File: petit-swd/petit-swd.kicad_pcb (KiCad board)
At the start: 2 copper layers, 11 parts, among them CON101 302-S201, CON102 61300411121, CON103 PPTC041LGBN-RC, CON104 USB-B1HSB6, CON105 61300311121, CON106 61300211121, U101 AZ1117CH-3.3TRG1

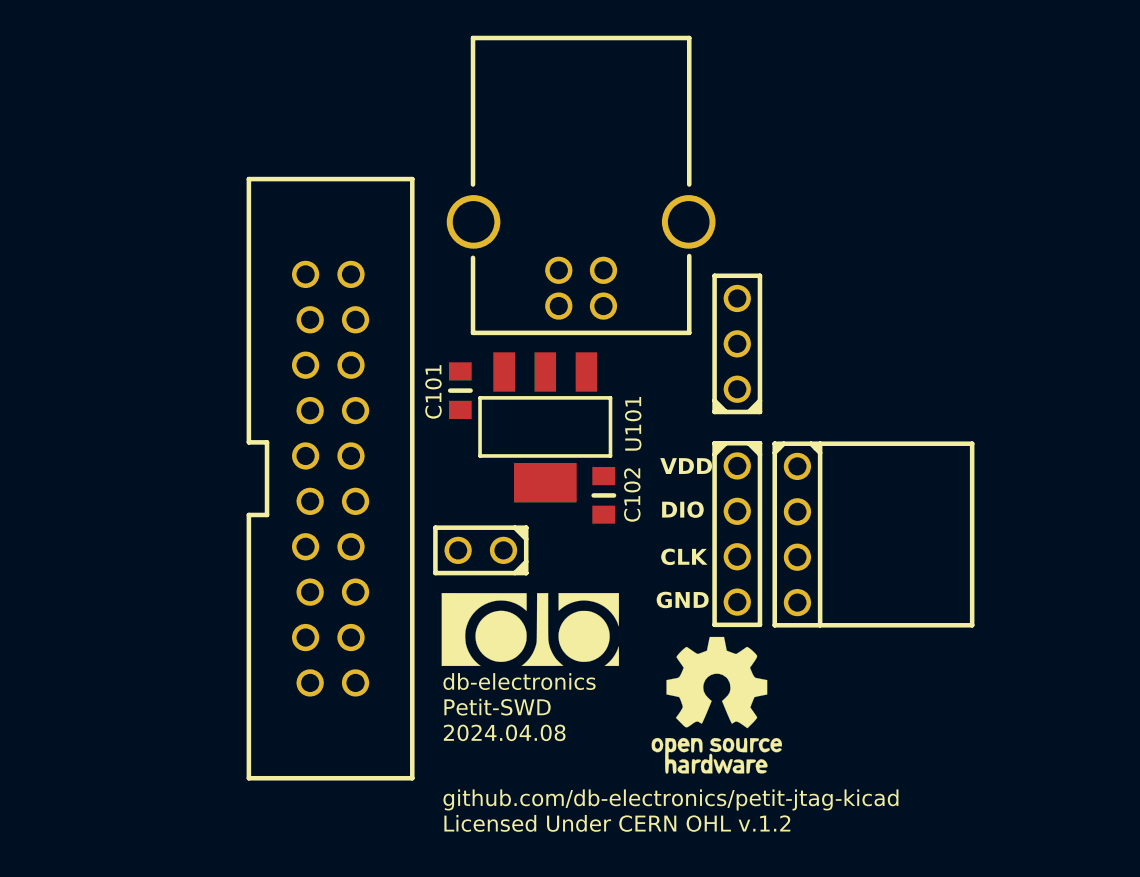
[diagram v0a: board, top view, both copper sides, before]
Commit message: swd v1.0 sch complete, jtag v1.1 files
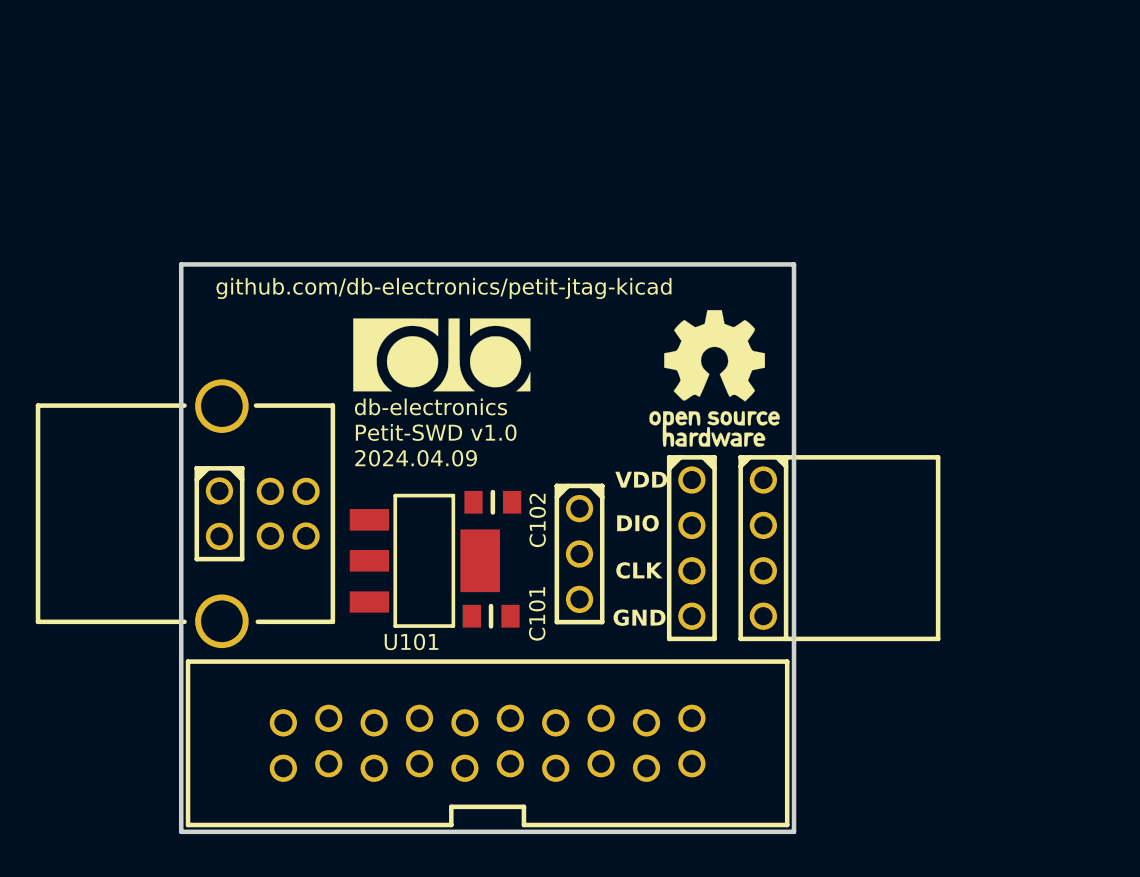
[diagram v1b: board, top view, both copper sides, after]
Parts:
- moved CON101 27.5 mm to (131.4, 108.1), turned to 90 degrees
- moved CON104 22.1 mm to (130.7, 94.0), turned to 90 degrees
- moved logo102 18.3 mm to (155.6, 86.4)
- moved CON106 16.2 mm to (127.9, 92.7), turned to 0 degrees
- moved logo101 16.1 mm to (140.3, 85.1)
- moved U101 14.4 mm to (136.3, 96.6), turned to -90 degrees
- moved C101 13.7 mm to (142.0, 99.7), turned to 0 degrees
- moved CON105 11.1 mm to (148.0, 93.7), turned to 0 degrees
- moved C102 7.43 mm to (142.1, 93.3), turned to 0 degrees
- moved CON102 2.66 mm to (154.3, 92.1)
- moved CON103 2.05 mm to (158.3, 92.1)
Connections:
- CON101 pad 1: VPP -> VCC
- CON101 pad 2: VPP -> VCC
- CON102 pad 1: VDD -> VCC
- CON103 pad 1: VDD -> VCC
- CON105 pad 2: VDD -> VCC
- CON106 pad 1: VDD -> +5V
- CON106 pad 2: VPP -> GND
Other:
- board outline added: 34.3 x 31.8 mm
- board text added: "db-electronics Petit-SWD v1.0 2024.04.09"
- board text added: "github.com/db-electronics/petit-jtag-kicad"
- board text removed: "db-electronics Petit-SWD 2024.04.08"
- board text removed: "github.com/db-electronics/petit-jtag-kicad Licensed Under CERN OHL v.1.2"
